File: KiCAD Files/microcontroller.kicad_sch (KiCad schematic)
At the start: 30 parts, among them IC5 AZ1117IH-3.3TRG1, J3 TSW-103-14-S-D, J4 TSW-103-14-S-D, U1 STM32H7A3RGTx, Y1 ABM8G-48.000MHZ-18-D2Y-T

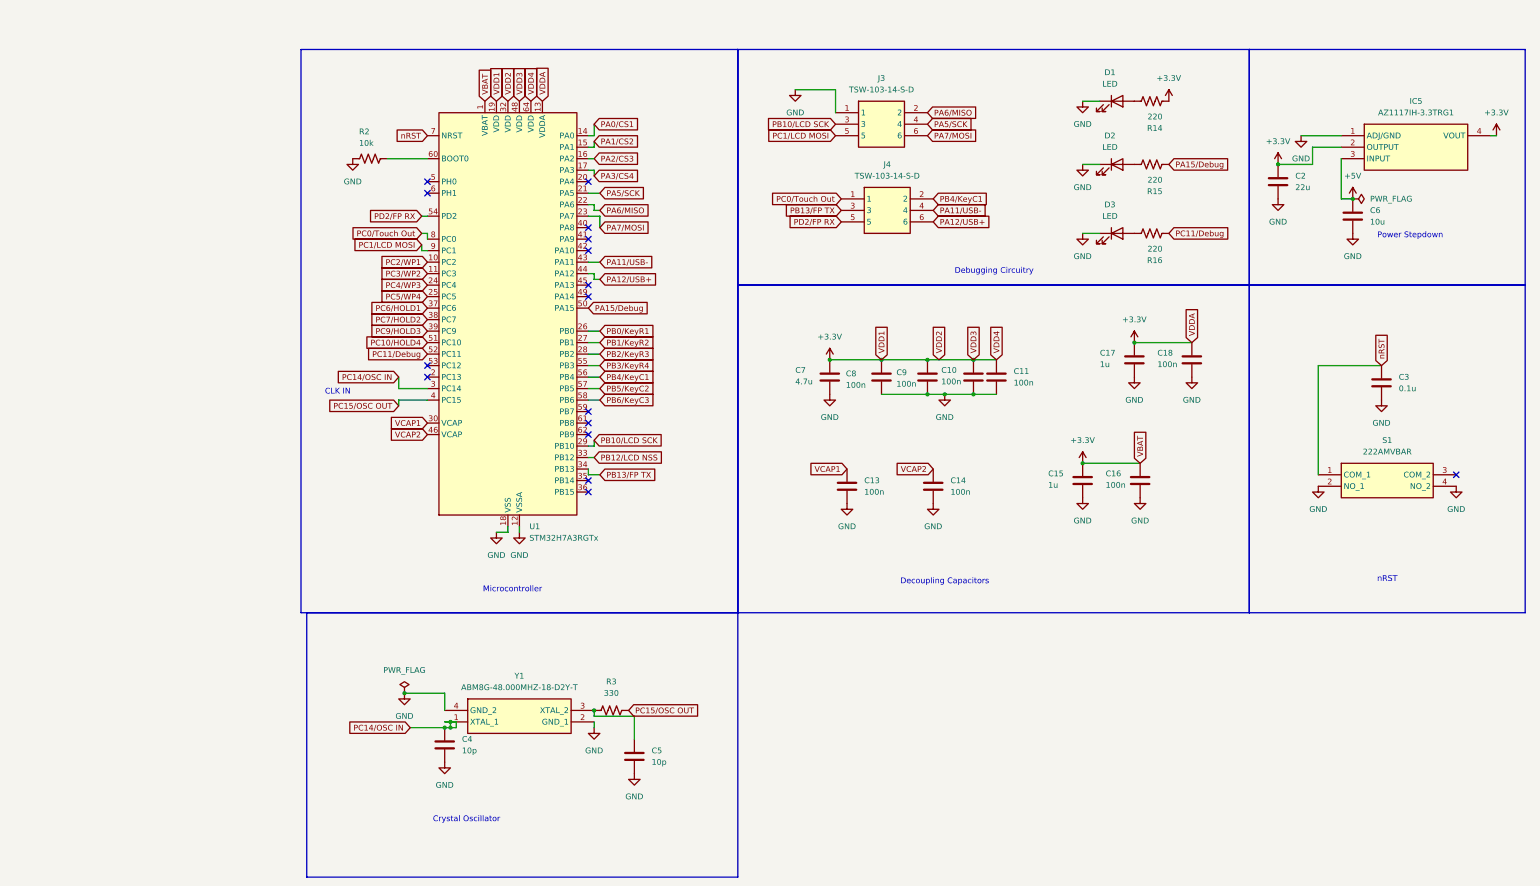
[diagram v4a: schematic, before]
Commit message: added testing points
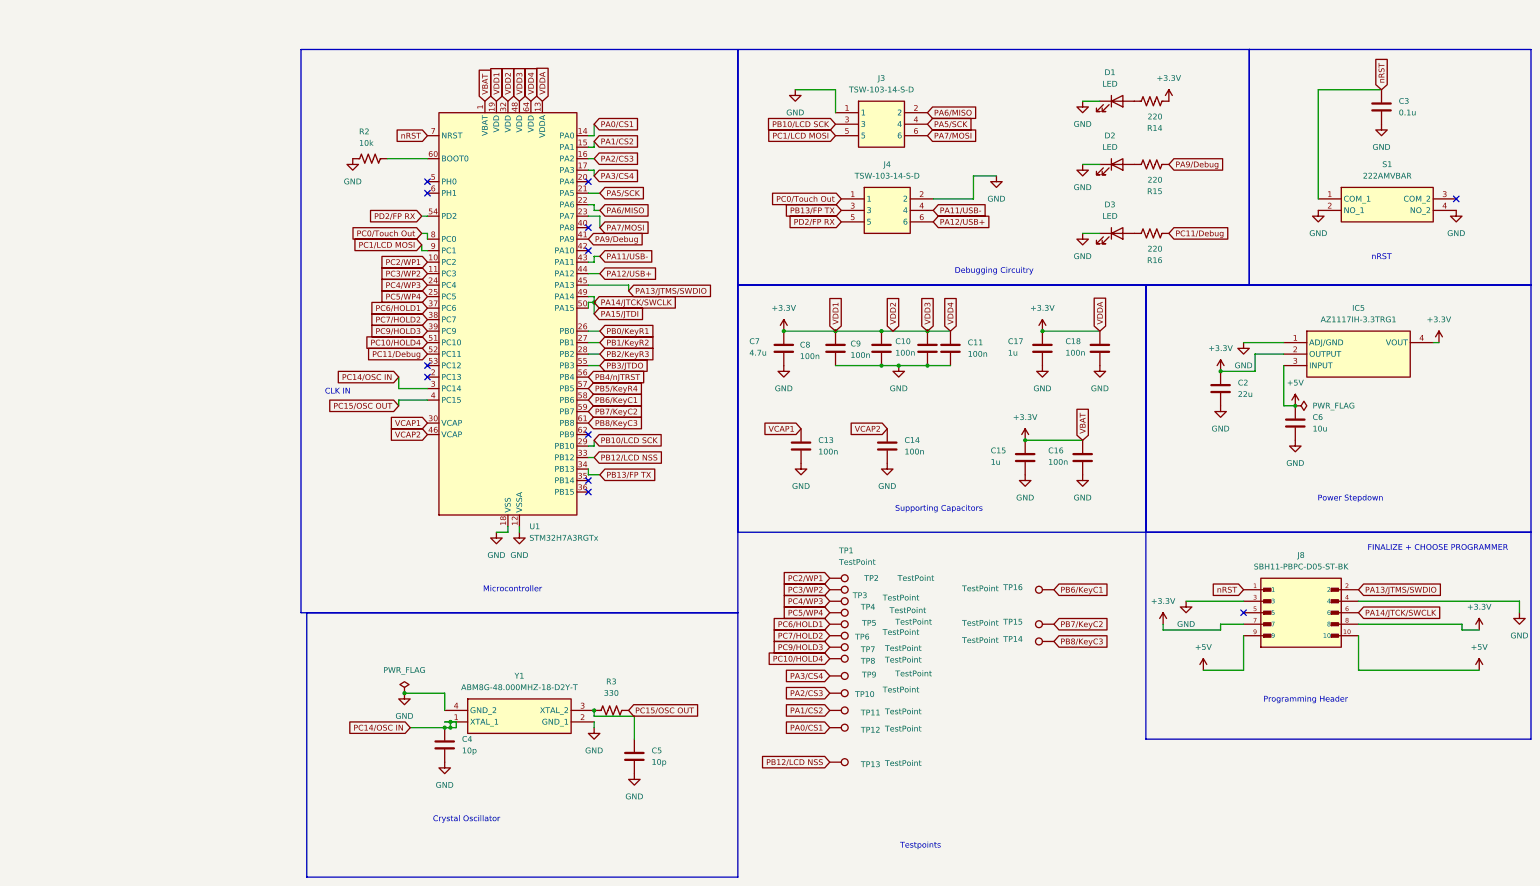
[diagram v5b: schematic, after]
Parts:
- added J8: SBH11-PBPC-D05-ST-BK, SBH11-PBPC-D05-ST-BK:SULLINS_SBH11-PBPC-D05-ST-BK, symbol CustomSymbols:SBH11-PBPC-D05-ST-BK
- added TP1, TP10, TP11, TP12, TP13, TP14, TP15, TP16, TP2, TP3, TP4, TP5, TP6, TP7, TP8, TP9: TestPoint, TestPoint:TestPoint_THTPad_D1.5mm_Drill0.7mm, symbol Connector:TestPoint
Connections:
- net +3.3V: now also J8.7, J8.8
- net +5V: now also J8.10, J8.9
- net GND: now also J4.2, J8.3, J8.4
- net PA0/CS1: now also TP12.1
- net PA1/CS2: now also TP11.1
- net PA2/CS3: now also TP10.1
- net PA3/CS4: now also TP9.1
- net PB12/LCD NSS: now also TP13.1
- net PC10/HOLD4: now also TP8.1
- net PC2/WP1: now also TP1.1
- net PC3/WP2: now also TP2.1
- net PC4/WP3: now also TP3.1
- net PC5/WP4: now also TP4.1
- net PC6/HOLD1: now also TP5.1
- net PC7/HOLD2: now also TP6.1
- net PC9/HOLD3: now also TP7.1
- net nRST: now also J8.1
- net PA9/Debug: now reaches U1.41 (PA9)
- net PA9/Debug: now also R15.2
- net PA13/JTMS/SWDIO: now reaches U1.45 (PA13)
- net PA13/JTMS/SWDIO: now also J8.2
- net PA14/JTCK/SWCLK: now reaches U1.49 (PA14)
- net PA14/JTCK/SWCLK: now also U1.50 (PA15), J8.6
- net PB7/KeyC2: now reaches U1.59 (PB7)
- net PB7/KeyC2: now also TP15.1
- net PB8/KeyC3: now reaches U1.61 (PB8)
- net PB8/KeyC3: now also TP14.1
- removed net PA15/Debug: R15.2, U1.50 (PA15)
- net PB3/KeyR4 renamed PB3/JTDO
- net PB4/KeyC1 renamed PB4/nJTRST
- net PB4/nJTRST: no longer J4.2
- net PB5/KeyC2 renamed PB5/KeyR4
- net PB6/KeyC3 renamed PB6/KeyC1
- net PB6/KeyC1: now also TP16.1
- no-connect marks 16 -> 12
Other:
- note added: "FINALIZE + CHOOSE PROGRAMMER"
- note added: "Programming Header"
- note added: "Supporting Capacitors"
- note added: "Testpoints"
- note removed: "Decoupling Capacitors"
- moved on the sheet: C10, C11, C13, C14, C15, C16, C17, C18, C3, C7, C8, C9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

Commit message: routed essential signals
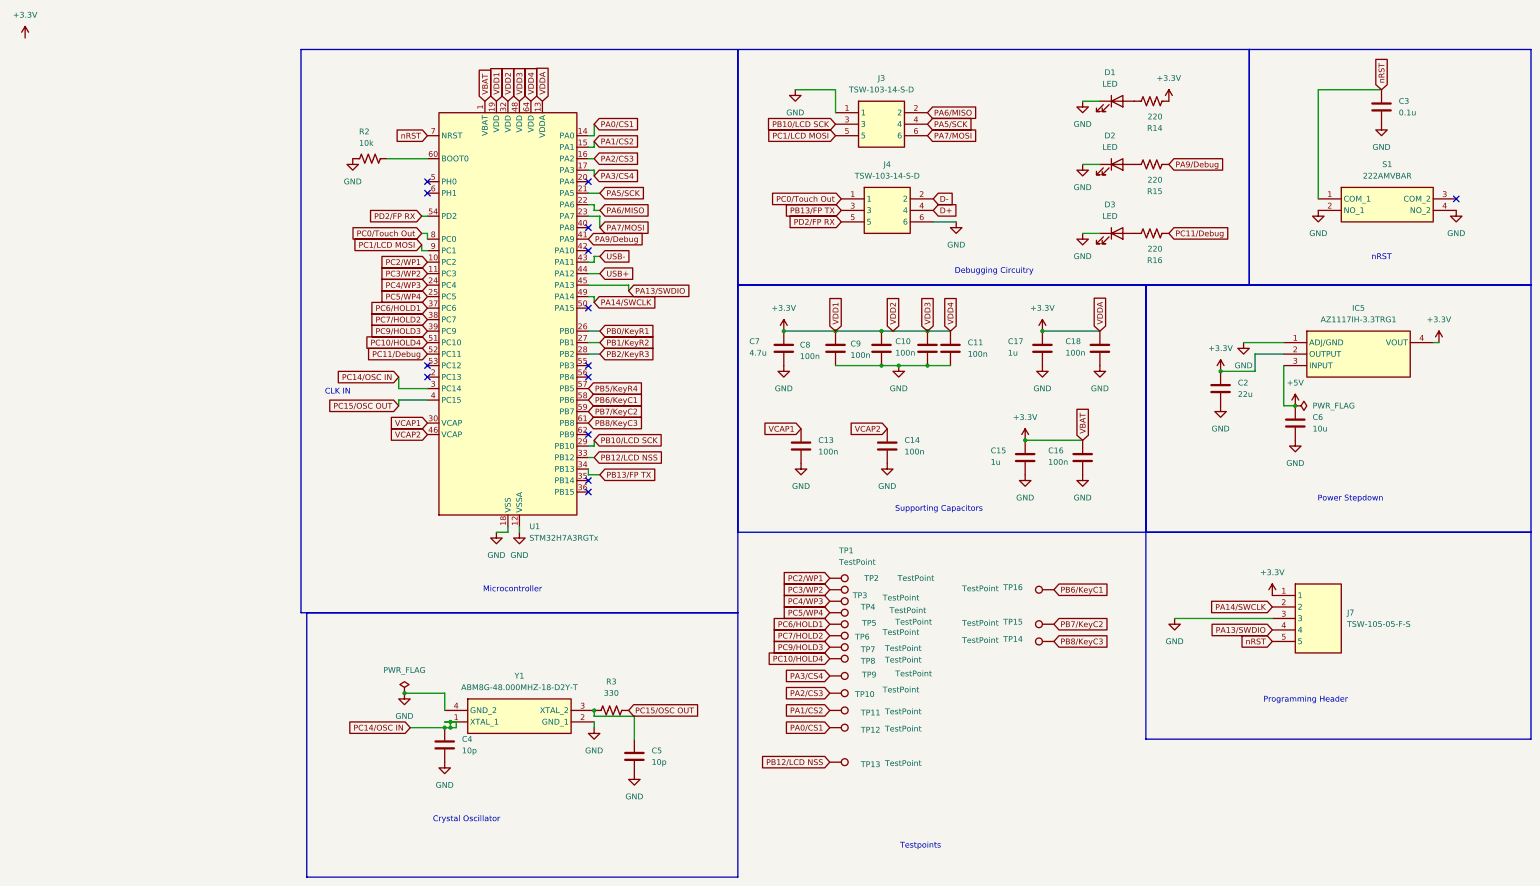
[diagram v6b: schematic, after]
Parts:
- removed J8: SBH11-PBPC-D05-ST-BK, SBH11-PBPC-D05-ST-BK:SULLINS_SBH11-PBPC-D05-ST-BK, symbol CustomSymbols:SBH11-PBPC-D05-ST-BK
- added J7: TSW-105-05-F-S, TSW-105-XX-YY-S, symbol CustomSymbols:TSW-105-05-F-S
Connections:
- net +3.3V: now also J7.1
- net GND: now also J4.6, J7.3; no longer J4.2
- net nRST: now also J7.5
- net PA11/USB- renamed D+
- net D+: no longer U1.43 (PA11)
- net PA12/USB+ renamed USB+
- net USB+: no longer J4.6
- net PA13/JTMS/SWDIO renamed PA13/SWDIO
- net PA13/SWDIO: now also J7.4
- net PA14/JTCK/SWCLK: no longer names the net of U1.50 (PA15)
- net PA14/JTCK/SWCLK: no longer U1.49 (PA14)
- net PB3/JTDO: no longer names the net of U1.55 (PB3)
- net PB4/nJTRST: no longer names the net of U1.56 (PB4)
- new net D-: J4.2
- new net PA14/SWCLK: J7.2, U1.49 (PA14)
- new net USB-: U1.43 (PA11)
- no-connect marks 12 -> 14
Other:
- note removed: "FINALIZE + CHOOSE PROGRAMMER"

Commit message: finished file
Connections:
- net PA0/CS1: no longer U1.14 (PA0)
- net PA1/CS2: no longer U1.15 (PA1)
- net PA2/CS3: no longer U1.16 (PA2)
- net PA3/CS4: no longer U1.17 (PA3)
- net PC10/HOLD4: no longer U1.51 (PC10)
- net PC2/WP1: no longer U1.10 (PC2)
- net PC4/WP3: no longer U1.24 (PC4)
- net PC5/WP4: no longer U1.25 (PC5)
- net PC7/HOLD2: no longer U1.38 (PC7)
- net PC9/HOLD3: no longer U1.39 (PC9)
- new net PA0/WP4: U1.14 (PA0)
- new net PA1/CS4: U1.15 (PA1)
- new net PA2/HOLD4: U1.16 (PA2)
- new net PA3/CS3: U1.17 (PA3)
- new net PC10/CS2: U1.51 (PC10)
- new net PC2/HOLD2: U1.10 (PC2)
- new net PC4/HOLD3: U1.24 (PC4)
- new net PC5/WP3: U1.25 (PC5)
- new net PC7/WP1: U1.38 (PC7)
- new net PC9/CS1: U1.39 (PC9)
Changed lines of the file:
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@@
 		)
 	)
-	(global_label "PC2{slash}WP1"
+	(global_label "PC2{slash}HOLD2"
 		(shape input)
 		(at 40.64 59.69 180)
@@
 		)
 		(property "Intersheetrefs" "${INTERSHEET_REFS}"
-			(at 28.6439 59.69 0)
+			(at 26.4062 59.69 0)
 			(effects
 				(font
@@
 		)
 	)
-	(global_label "PA0{slash}CS1"
+	(global_label "PA0{slash}WP4"
 		(shape input)
 		(at 77.47 29.21 0)
@@
 		)
 		(property "Intersheetrefs" "${INTERSHEET_REFS}"
-			(at 89.0428 29.21 0)
+			(at 89.2847 29.21 0)
 			(effects
 				(font
@@
 		)
 	)
-	(global_label "PC5{slash}WP4"
+	(global_label "PC5{slash}WP3"
 		(shape input)
 		(at 40.64 67.31 180)
@@
 		)
 	)
-	(global_label "PA3{slash}CS4"
+	(global_label "PA3{slash}CS3"
 		(shape input)
 		(at 77.47 40.64 0)
@@
 		)
 	)
-	(global_label "PC7{slash}HOLD2"
+	(global_label "PC7{slash}WP1"
 		(shape input)
 		(at 40.64 72.39 180)
@@
 		)
 		(property "Intersheetrefs" "${INTERSHEET_REFS}"
-			(at 26.4062 72.39 0)
+			(at 28.6439 72.39 0)
 			(effects
 				(font
@@
 		)
 	)
-	(global_label "PC10{slash}HOLD4"
+	(global_label "PC10{slash}CS2"
 		(shape input)
 		(at 40.64 77.47 180)
@@
 		)
 		(property "Intersheetrefs" "${INTERSHEET_REFS}"
-			(at 25.1967 77.47 0)
+			(at 27.6763 77.47 0)
 			(effects
 				(font
@@
 		)
 	)
-	(global_label "PC4{slash}WP3"
+	(global_label "PC4{slash}HOLD3"
 		(shape input)
 		(at 40.64 64.77 180)
@@
 		)
 		(property "Intersheetrefs" "${INTERSHEET_REFS}"
-			(at 28.6439 64.77 0)
+			(at 26.4062 64.77 0)
 			(effects
 				(font
@@
 		)
 	)
-	(global_label "PA1{slash}CS2"
+	(global_label "PA1{slash}CS4"
 		(shape input)
 		(at 77.47 33.02 0)
@@
 		)
 	)
-	(global_label "PC9{slash}HOLD3"
+	(global_label "PC9{slash}CS1"
 		(shape input)
 		(at 40.64 74.93 180)
@@
 		)
 		(property "Intersheetrefs" "${INTERSHEET_REFS}"
-			(at 26.4062 74.93 0)
+			(at 28.8858 74.93 0)
 			(effects
 				(font
@@
 		)
 	)
-	(global_label "PA2{slash}CS3"
+	(global_label "PA2{slash}HOLD4"
 		(shape input)
 		(at 77.47 36.83 0)
@@
 		)
 		(property "Intersheetrefs" "${INTERSHEET_REFS}"
-			(at 89.0428 36.83 0)
+			(at 91.5224 36.83 0)
 			(effects
 				(font
@@
 					(unit 1)
 				)
-			)
-		)
-	)
-	(symbol
-		(lib_id "CustomSymbols:+3.3V")
-		(at -48.26 10.16 0)
-		(unit 1)
-		(exclude_from_sim no)
-		(in_bom yes)
-		(on_board yes)
-		(dnp no)
-		(fields_autoplaced yes)
-		(property "Reference" "#PWR051"
-			(at -48.26 13.97 0)
-			(effects
-				(font
-					(size 1.27 1.27)
-				)
-				(hide yes)
-			)
-		)
-		(property "Value" "+3.3V"
-			(at -48.26 5.08 0)
-			(effects
-				(font
-					(size 1.27 1.27)
-				)
-			)
-		)
-		(property "Footprint" ""
-			(at -48.26 10.16 0)
-			(effects
-				(font
-					(size 1.27 1.27)
-				)
-				(hide yes)
-			)
-		)
-		(property "Datasheet" ""
-			(at -48.26 10.16 0)
-			(effects
-				(font
-					(size 1.27 1.27)
-				)
-				(hide yes)
-			)
-		)
-		(property "Description" "Power symbol creates a global label with name \"+3.3V\""
-			(at -48.26 10.16 0)
-			(effects
-				(font
-					(size 1.27 1.27)
-				)
-				(hide yes)
-			)
-		)
-		(pin "1"
-		)
-		(instances
-			(project ""
-				(path "/b633f67e-3a02-4f0f-b079-02d1853b4f15/e8b68c2d-7a8c-4c60-b0ed-d46a3d1cc27a"
-					(reference "#PWR051")
-					(unit 1)
-				)

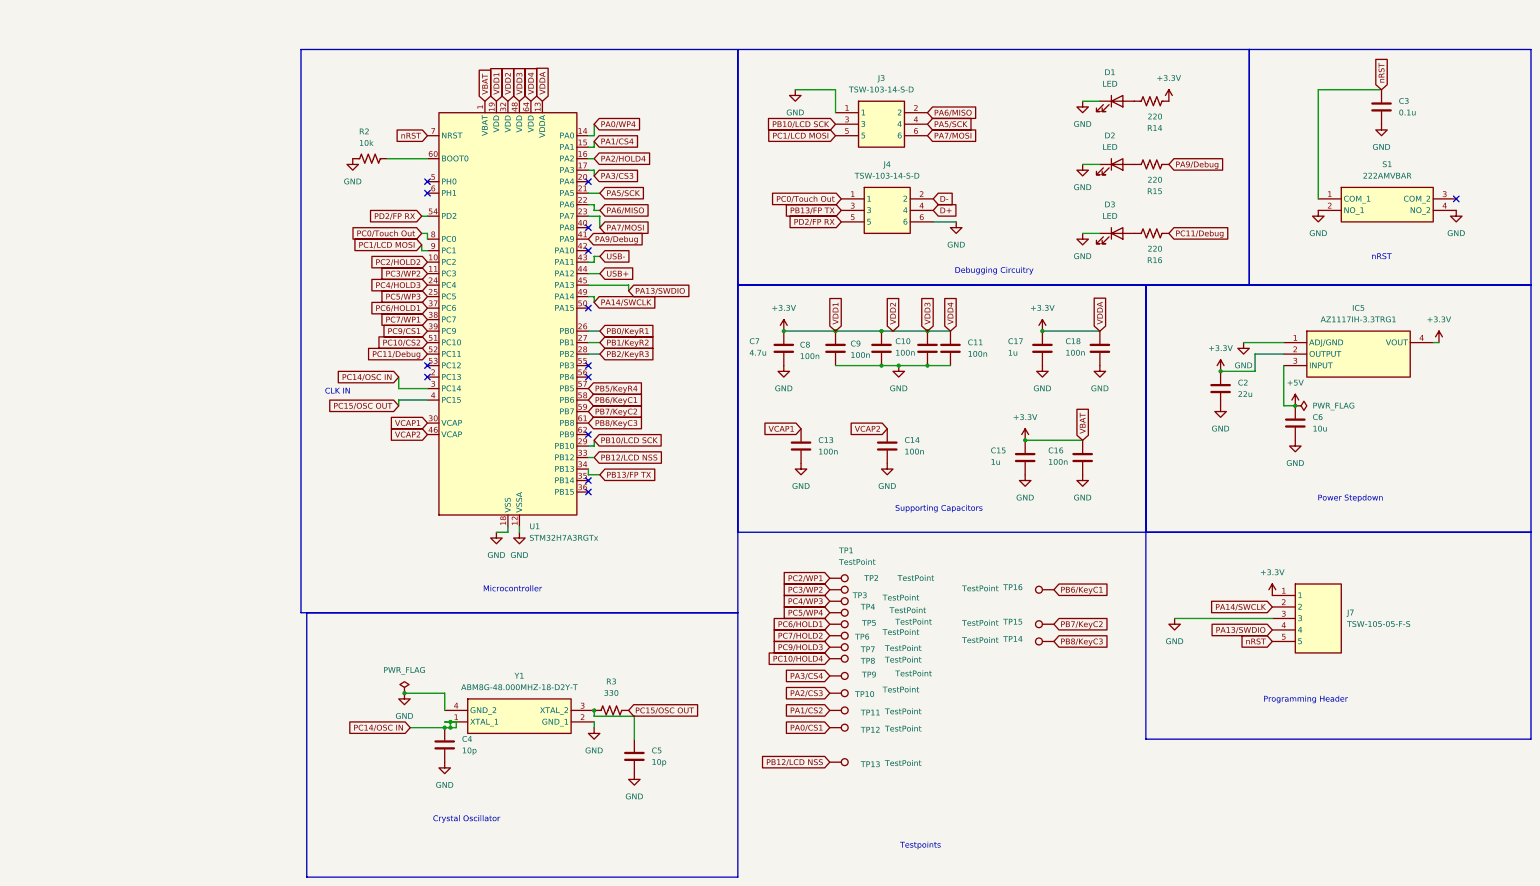
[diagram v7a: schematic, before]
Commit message: Finalized Signal Routing
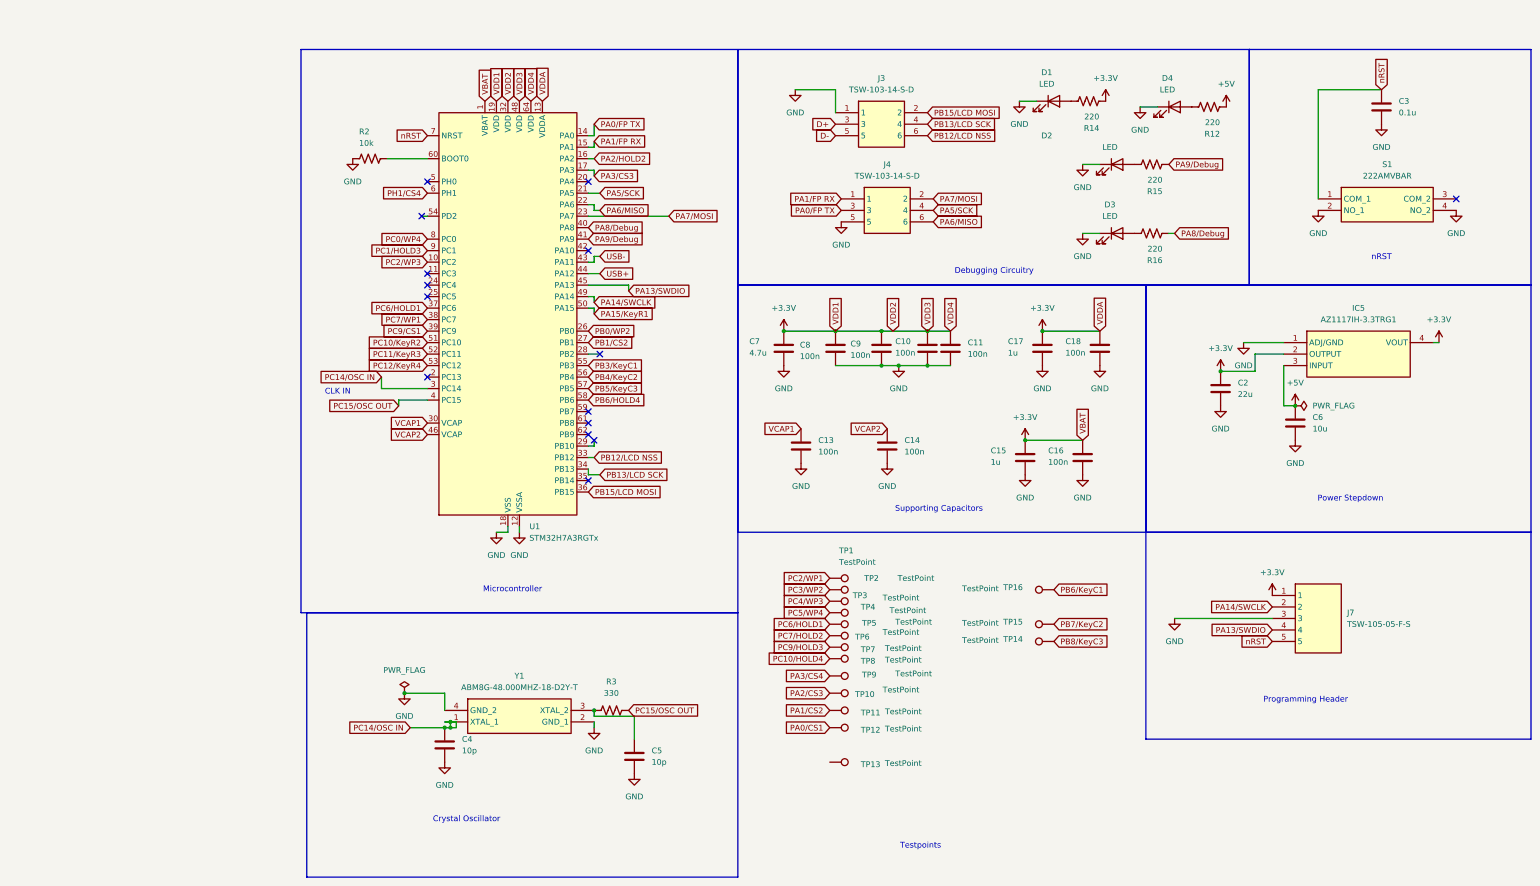
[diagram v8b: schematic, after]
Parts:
- added D4: LED, LED_SMD:LED_0805_2012Metric_Pad1.15x1.40mm_HandSolder, symbol Device:LED
- added R12: 220, Resistor_SMD:R_0805_2012Metric_Pad1.20x1.40mm_HandSolder, symbol CustomSymbols:R_US
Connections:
- net +5V: now also R12.2
- net D+: now also J3.3; no longer J4.4
- net D-: now also J3.5; no longer J4.2
- net GND: now also J4.5, D4.1 (K); no longer J4.6
- net PA5/SCK: now also J4.4; no longer J3.4
- net PA6/MISO: now also J4.6; no longer J3.2
- net PA7/MOSI: now also J4.2; no longer J3.6
- net PB12/LCD NSS: now also J3.6; no longer TP13.1
- net PB6/KeyC1: no longer U1.58 (PB6)
- net PB7/KeyC2: no longer U1.59 (PB7)
- net PB8/KeyC3: no longer U1.61 (PB8)
- net PC3/WP2: no longer U1.11 (PC3)
- net PB15/LCD MOSI: now reaches U1.36 (PB15)
- net PB15/LCD MOSI: now also J3.2
- net PA8/Debug: now reaches U1.40 (PA8)
- net PA8/Debug: now also R16.2
- net PA15/KeyR1: now reaches U1.50 (PA15)
- net PC12/KeyR4: now reaches U1.53 (PC12)
- net PB3/KeyC1: now reaches U1.55 (PB3)
- net PB4/KeyC2: now reaches U1.56 (PB4)
- net PH1/CS4: now reaches U1.6 (PH1)
- net PA0/WP4 renamed PA0/FP TX
- net PA0/FP TX: now also J4.3
- net PA1/CS4 renamed PA1/FP RX
- net PA1/FP RX: now also J4.1
- net PA2/HOLD4 renamed PA2/HOLD2
- net PB0/KeyR1 renamed PB0/WP2
- net PB10/LCD SCK: no longer names the net of U1.29 (PB10)
- net PB10/LCD SCK: no longer J3.3
- net PB13/FP TX renamed PB13/LCD SCK
- net PB13/LCD SCK: now also J3.4; no longer J4.3
- net PB1/KeyR2 renamed PB1/CS2
- net PB2/KeyR3: no longer names the net of U1.28 (PB2)
- net PB5/KeyR4 renamed PB5/KeyC3
- net PC0/Touch Out renamed PC0/WP4
- net PC0/WP4: no longer J4.1
- net PC10/CS2 renamed PC10/KeyR2
- net PC11/Debug renamed PC11/KeyR3
- net PC11/KeyR3: no longer R16.2
- net PC1/LCD MOSI renamed PC1/HOLD3
- net PC1/HOLD3: no longer J3.5
- net PC2/HOLD2 renamed PC2/WP3
- net PC4/HOLD3: no longer names the net of U1.24 (PC4)
- net PC5/WP3: no longer names the net of U1.25 (PC5)
- net PD2/FP RX: no longer names the net of U1.54 (PD2)
- net PD2/FP RX: no longer J4.5
- new net: D4.2 (A), R12.1
- new net PB6/HOLD4: U1.58 (PB6)
- no-connect marks 14 -> 15
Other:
- moved on the sheet: D1, R14
